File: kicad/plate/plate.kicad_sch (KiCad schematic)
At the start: 52 parts, among them SW1 EC_SW

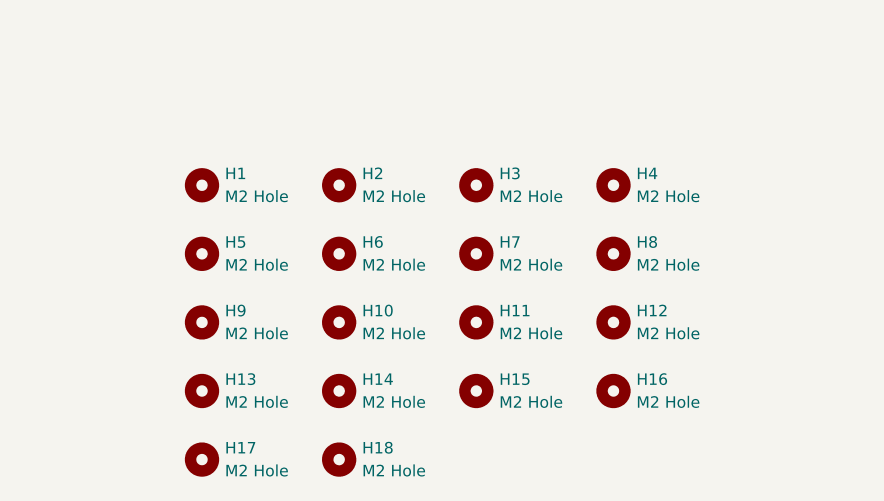
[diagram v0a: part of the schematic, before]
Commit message: Clean up after prototyping
- Doc update
- remove uncessary files
- remove two more mounting holes in the "chiffre gap" area
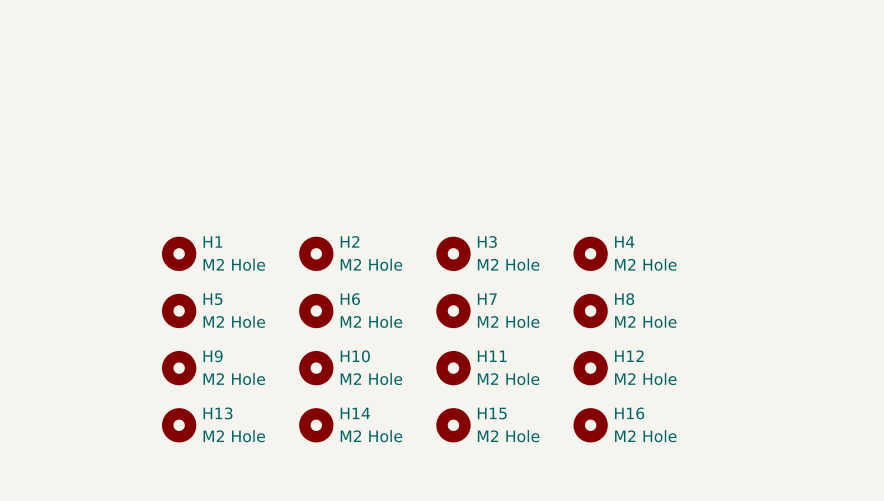
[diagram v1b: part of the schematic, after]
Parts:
- removed H17, H18: M2 Hole, capacitive_sensors:MountingHole_1.6mm_M2_tapped, symbol Mechanical:MountingHole
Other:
- moved on the sheet: H1, H2, H3, H4

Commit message: Remove extra mounting holes from PCB and update version number.
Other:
- title: Le Capybara -> Le Capybara Plate
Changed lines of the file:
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@@
   (paper "A4")
   (title_block
-    (title "Le Capybara")
-    (date "2023-07-08")
-    (rev "0.2")
+    (title "Le Capybara Plate")
+    (date "2024-02-21")
+    (rev "1.0")
     (company "sporkus")
   )
